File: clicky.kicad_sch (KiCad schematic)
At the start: 14 parts, among them J1 OLED_128x64, U1 RP2040_Zero

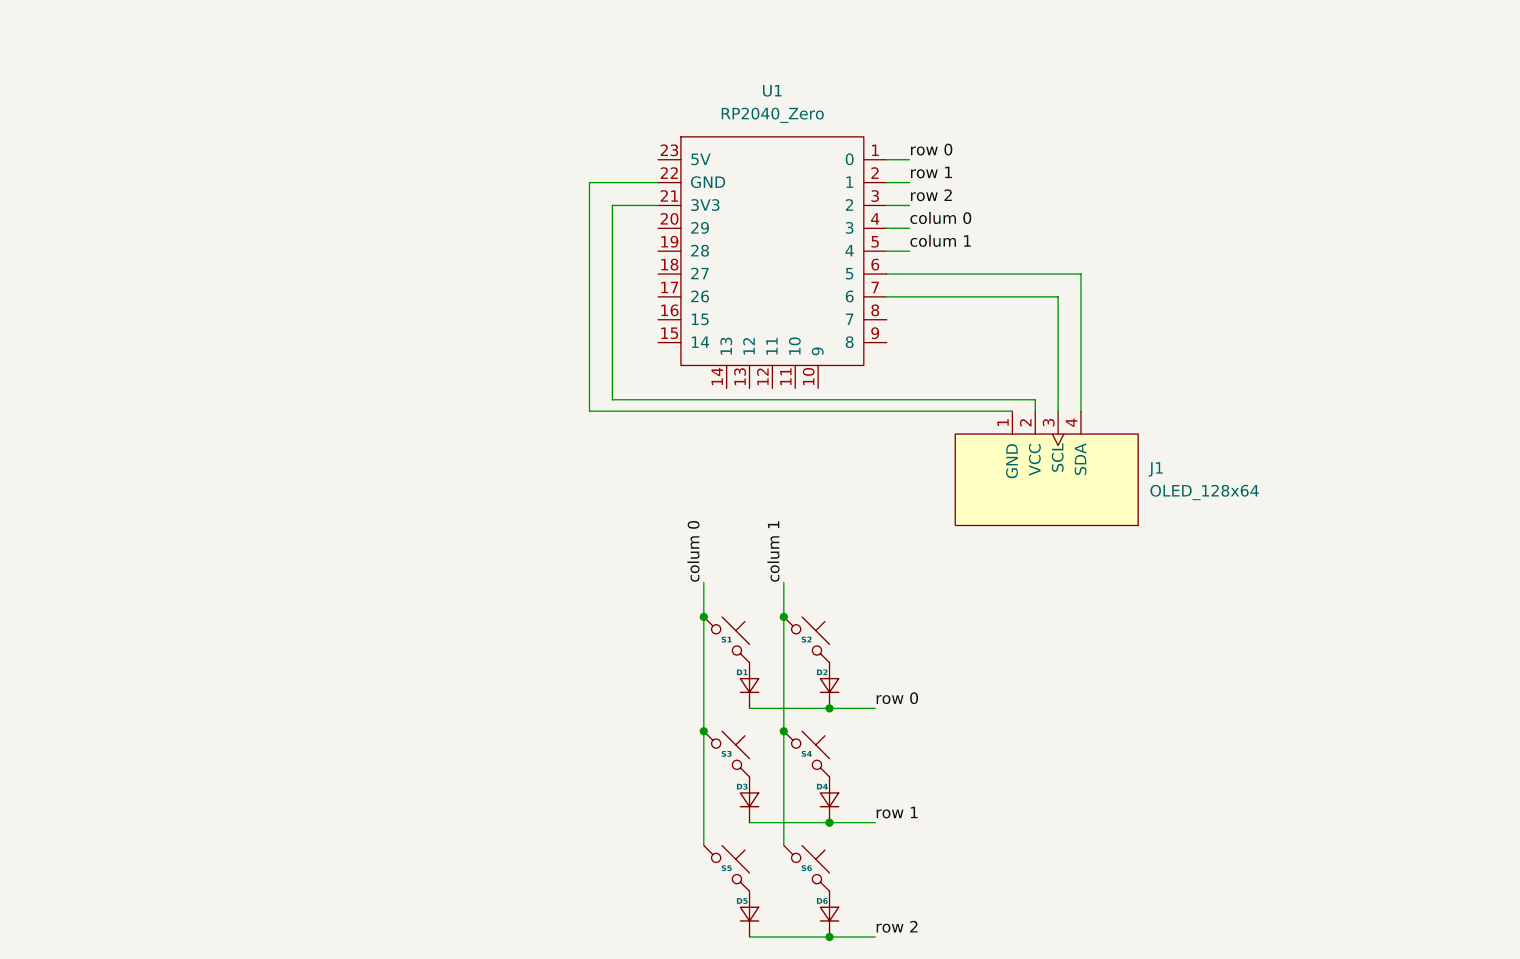
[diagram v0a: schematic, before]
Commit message: Scaffold Arduino firmware, add board render and fix wiring
- firmware/: Arduino IDE scaffold (clicky.ino mood state machine, pins.h,
  moods.h), TFT_eSPI GC9A01 setup, and Arduino IDE setup guide. Compiles
  clean for the XIAO ESP32-C3.
- assets/: single 2D capture of the fully-placed PCB, shown in the README.
- README: board preview image; correct DS18B20 pin (D7, not D6) derived
  from the schematic netlist; firmware + status updates.
- .gitignore: exclude history plugin state and regenerable KiCad exports.
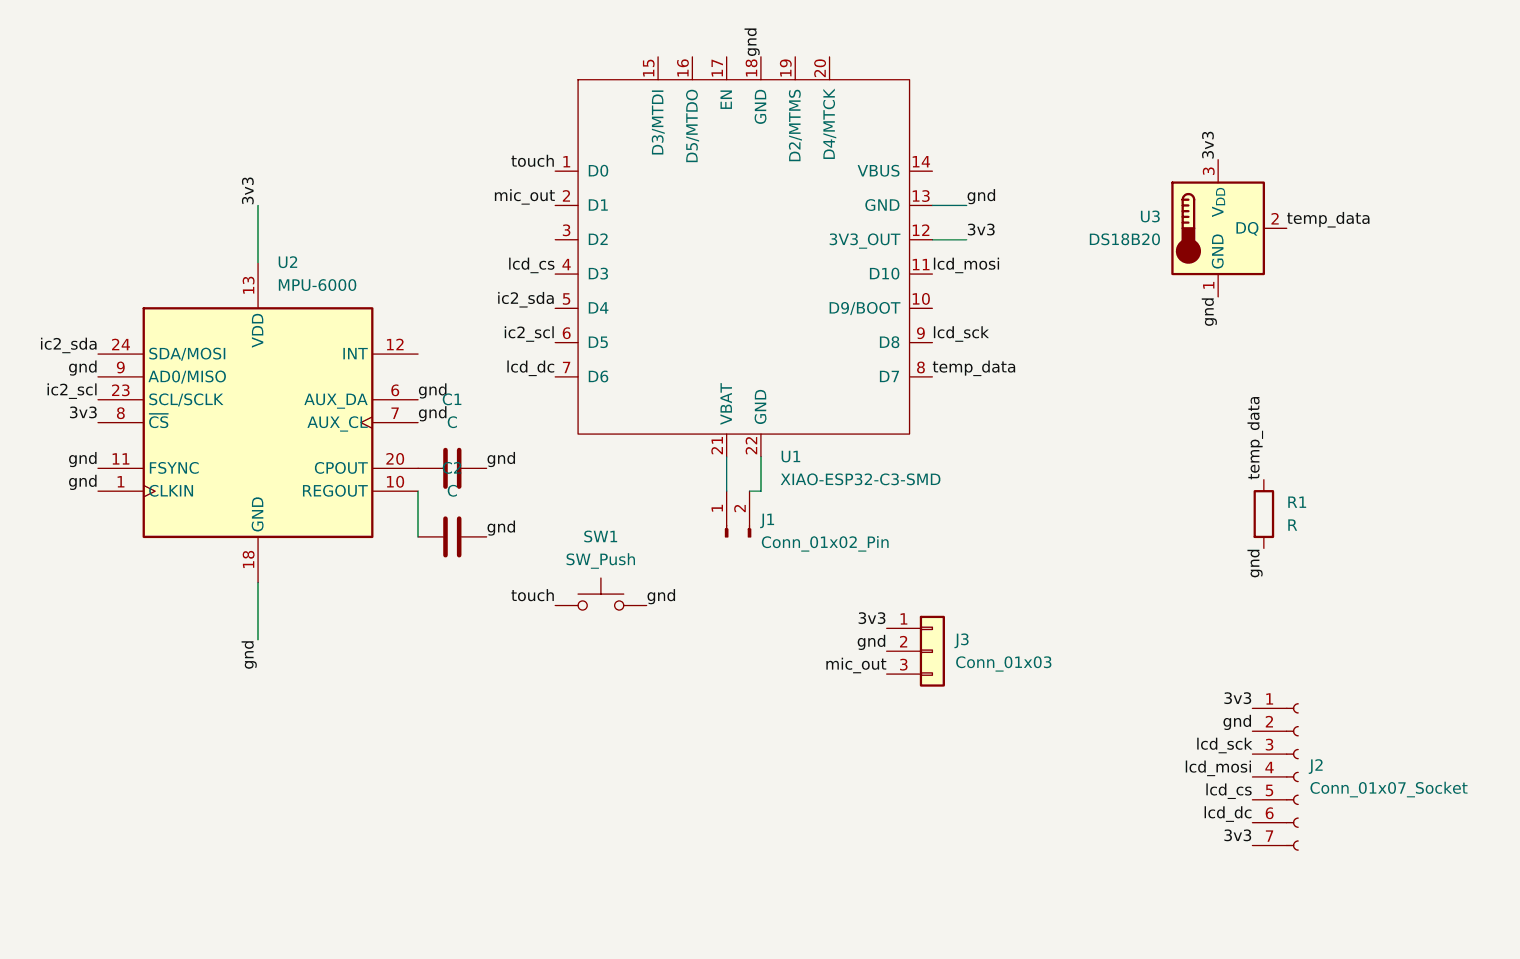
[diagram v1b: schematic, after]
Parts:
- removed D1, D2, D3, D4, D5, D6: (no value), ScottoKeebs_Components:Diode_DO-35, symbol ScottoKeebs:Placeholder_Diode
- removed J1: OLED_128x64, ScottoKeebs_Components:OLED_128x64, symbol ScottoKeebs:OLED_128x64
- removed S1, S2, S3, S4, S5, S6: (no value), ScottoKeebs_MX:MX_PCB_1.00u, symbol ScottoKeebs:Placeholder_Keyswitch
- removed U1: RP2040_Zero, ScottoKeebs_MCU:RP2040_Zero, symbol ScottoKeebs:MCU_RP2040_Zero
- added C1, C2: C, Capacitor_SMD:C_0603_1608Metric, symbol Device:C
- added J1: Conn_01x02_Pin, Connector_JST:JST_PH_B2B-PH-K_1x02_P2.00mm_Vertical, symbol Connector:Conn_01x02_Pin
- added J2: Conn_01x07_Socket, Connector_PinHeader_2.54mm:PinHeader_1x07_P2.54mm_Vertical, symbol Connector:Conn_01x07_Socket
- added J3: Conn_01x03, Connector_PinHeader_2.54mm:PinHeader_1x03_P2.54mm_Vertical, symbol Connector_Generic:Conn_01x03
- added R1: R, Resistor_THT:R_Axial_DIN0207_L6.3mm_D2.5mm_P10.16mm_Horizontal, symbol Device:R
- added SW1: SW_Push, Button_Switch_THT:SW_NKK_GW12LJP, symbol Switch:SW_Push
- added U1: XIAO-ESP32-C3-SMD, Seeed_Studio_XIAO_Series:XIAO-ESP32-C3-SMD, symbol Seeed_XIAO:XIAO-ESP32-C3-SMD
- added U2: MPU-6000, Sensor_Motion:InvenSense_QFN-24_4x4mm_P0.5mm, symbol Sensor_Motion:MPU-6000
- added U3: DS18B20, Package_TO_SOT_THT:TO-92_Inline, symbol Sensor_Temperature:DS18B20
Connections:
- new net: J1.1 (Pin_1), U1.21 (VBAT)
- new net: J1.2 (Pin_2), U1.22 (GND)
- new net: C1.2, U2.20 (CPOUT)
- new net: C2.2, U2.10 (REGOUT)
- new net 3v3: J2.1 (Pin_1), J2.7 (Pin_7), J3.1 (Pin_1), U1.12 (3V3_OUT), U2.13 (VDD), U2.8 (~{CS}), U3.3 (V_{DD})
- new net gnd: C1.1, C2.1, J2.2 (Pin_2), J3.2 (Pin_2), R1.2, SW1.2, U1.13 (GND), U1.18 (GND), U2.1 (CLKIN), U2.11 (FSYNC), U2.18 (GND), U2.6 (AUX_DA), U2.7 (AUX_CL), U2.9 (AD0/MISO), U3.1 (GND)
- new net ic2_scl: U1.6 (D5), U2.23 (SCL/SCLK)
- new net ic2_sda: U1.5 (D4), U2.24 (SDA/MOSI)
- new net lcd_cs: J2.5 (Pin_5), U1.4 (D3)
- new net lcd_dc: J2.6 (Pin_6), U1.7 (D6)
- new net lcd_mosi: J2.4 (Pin_4), U1.11 (D10)
- new net lcd_sck: J2.3 (Pin_3), U1.9 (D8)
- new net mic_out: J3.3 (Pin_3), U1.2 (D1)
- new net temp_data: R1.1, U1.8 (D7), U3.2 (DQ)
- new net touch: SW1.1, U1.1 (D0)

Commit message: Update README: add schematic & PCB images, drop Status section; commit R1 pull-up fix sources
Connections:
- net 3v3: now also R1.2
- net gnd: no longer R1.2
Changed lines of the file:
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@@
-		)
-	)
-	(label "gnd"
-		(at 186.69 100.33 270)
-		(effects
-			(font
-				(size 1.27 1.27)
-			)
-			(justify right bottom)
 		)
 	)
@@
 		(effects
 			(font
+				(size 1.27 1.27)
+			)
+			(justify right bottom)
+		)
+	)
+	(label "3v3"
+		(at 186.69 100.33 270)
+		(effects
+			(font
